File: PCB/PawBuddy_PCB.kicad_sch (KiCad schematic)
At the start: 1 part, among them U6 SHT4x

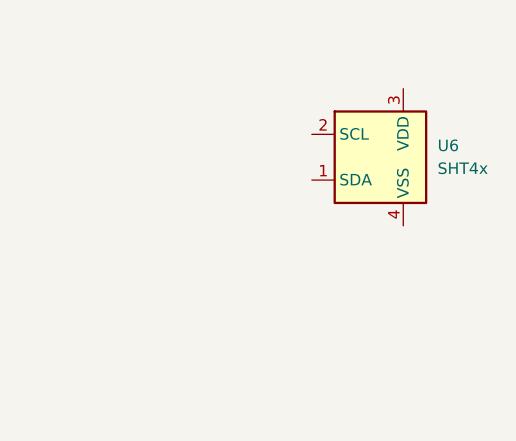
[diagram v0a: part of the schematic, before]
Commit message: added power block, pheripherial
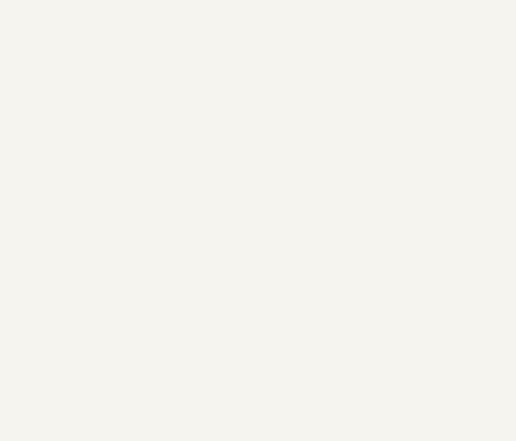
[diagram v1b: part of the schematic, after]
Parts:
- removed U6: SHT4x, Sensor_Humidity:Sensirion_DFN-4_1.5x1.5mm_P0.8mm_SHT4x_NoCentralPad, symbol Sensor_Humidity:SHT4x
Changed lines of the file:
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@@
 		(company "Tomas Kuchta")
-	)
-	(symbol
-		(lib_id "Sensor_Humidity:SHT4x")
-		(at 229.87 85.09 0)
-		(unit 1)
-		(body_style 1)
-		(exclude_from_sim no)
-		(in_bom yes)
-		(on_board yes)
-		(in_pos_files yes)
-		(dnp no)
-		(fields_autoplaced yes)
-		(property "Reference" "U6"
-			(at 236.22 83.8199 0)
-			(show_name no)
-			(do_not_autoplace no)
-			(effects
-				(font
-					(size 1.27 1.27)
-				)
-				(justify left)
-			)
-		)
-		(property "Value" "SHT4x"
-			(at 236.22 86.3599 0)
-			(show_name no)
-			(do_not_autoplace no)
-			(effects
-				(font
-					(size 1.27 1.27)
-				)
-				(justify left)
-			)
-		)
-		(property "Footprint" "Sensor_Humidity:Sensirion_DFN-4_1.5x1.5mm_P0.8mm_SHT4x_NoCentralPad"
-			(at 233.68 91.44 0)
-			(hide yes)
-			(show_name no)
-			(do_not_autoplace no)
-			(effects
-				(font
-					(size 1.27 1.27)
-				)
-				(justify left)
-			)
-		)
-		(property "Datasheet" "https://sensirion.com/media/documents/33FD6951/624C4357/Datasheet_SHT4x.pdf"
-			(at 233.68 93.98 0)
-			(hide yes)
-			(show_name no)
-			(do_not_autoplace no)
-			(effects
-				(font
-					(size 1.27 1.27)
-				)
-				(justify left)
-			)
-		)
-		(property "Description" "Digital Humidity and Temperature Sensor, ±1%RH, ±0.1°C, I2C, 1.08-3.6V, 16bit, DFN-4"
-			(at 229.87 85.09 0)
-			(hide yes)
-			(show_name no)
-			(do_not_autoplace no)
-			(effects
-				(font
-					(size 1.27 1.27)
-				)
-			)
-		)
-		(pin "3"
-		)
-		(pin "2"
-		)
-		(pin "4"
-		)
-		(pin "1"
-		)
-		(instances
-			(project "PawBuddy_PCB"
-				(path "/ddc031a5-f801-471f-9629-7d18bb02ea71"
-					(reference "U6")
-					(unit 1)
-				)
-			)
-		)
 	)
 	(sheet
